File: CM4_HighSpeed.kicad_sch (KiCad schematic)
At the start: 8 parts, among them J12 THD-02-R

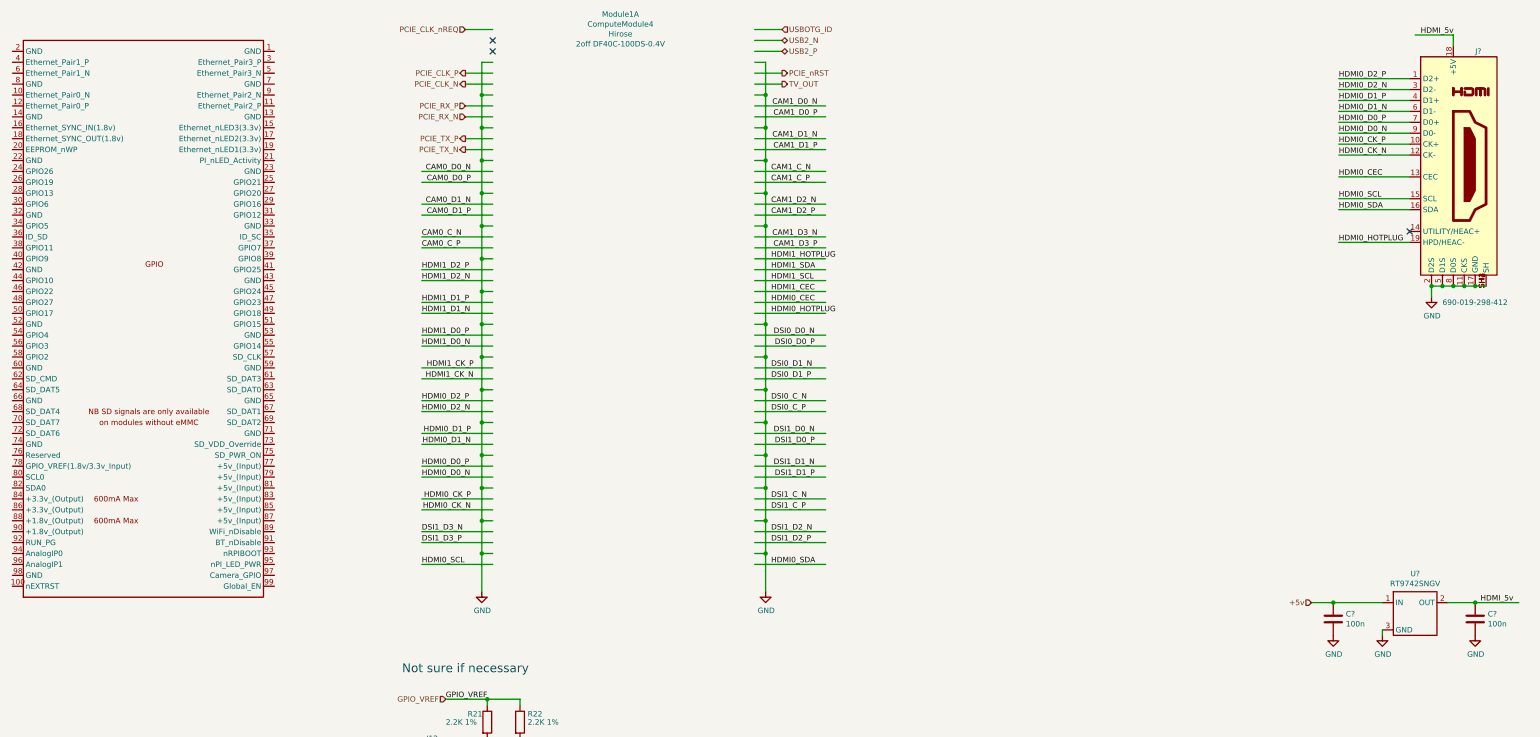
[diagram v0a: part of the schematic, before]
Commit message: Added footprints and symbols
Could not find -on SnapEDA- MCWR06X3322FTL, MCMR06X3162FTL and USB-A-S-VT.
Power load switch NCP380HSN05AAT1G only had footprint on SnapEDA, no symbol.
Need to update HMDI footprint and symbol to correct one.
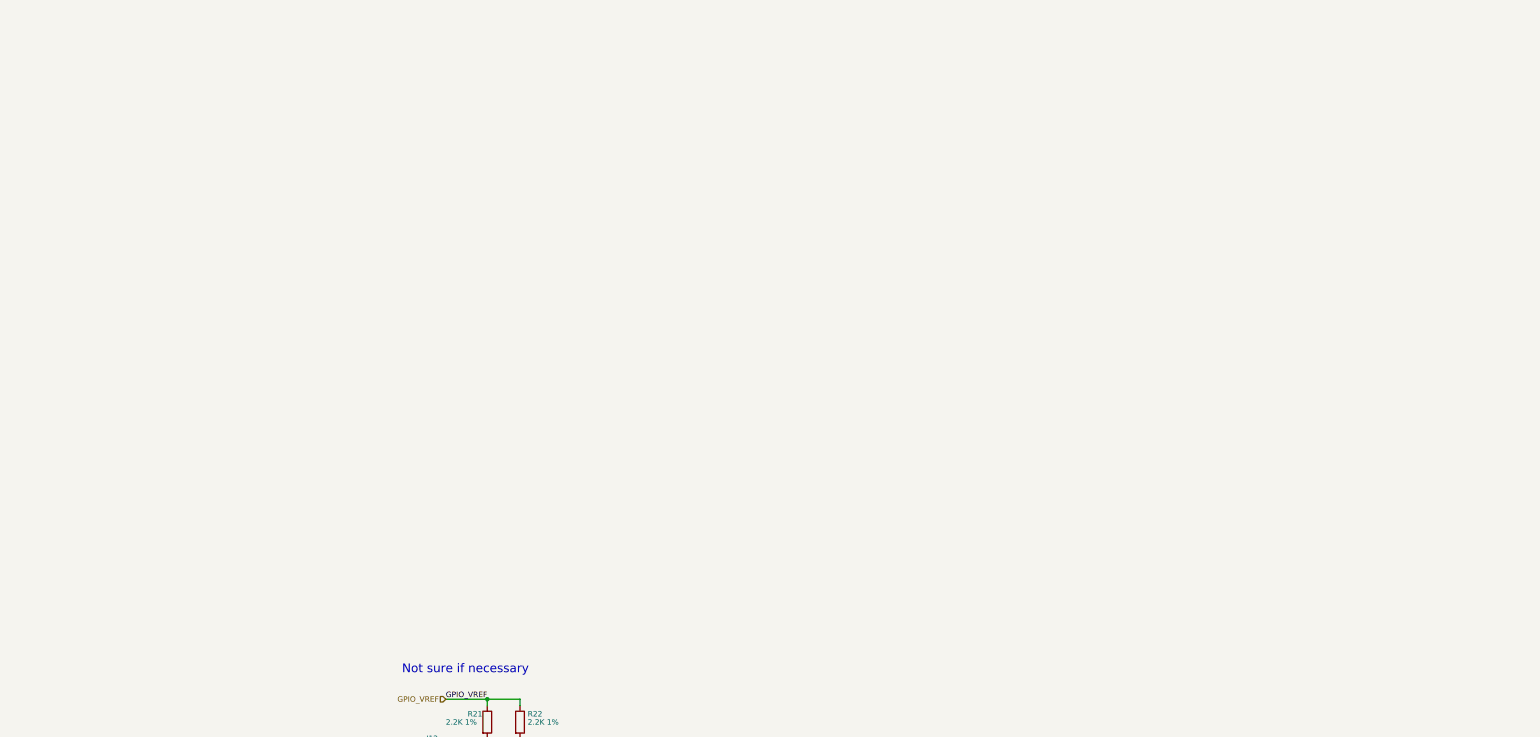
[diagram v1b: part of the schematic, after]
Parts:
- removed C? (x2): 100n, Capacitor_SMD:C_0402_1005Metric, symbol Device:C
- removed J?: 690-019-298-412, CM4IO:EDAC 690-019-298-412, symbol CM4IO:HDMI_A_1.4
- removed Module1: ComputeModule4, CM4IO:Raspberry-Pi-4-Compute-Module, symbol CM4IO:ComputeModule4-CM4
- removed U?: RT9742SNGV, Package_TO_SOT_SMD:SOT-23, symbol CM4IO:RT9742SNGV
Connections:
- no-connect marks 3 -> 0

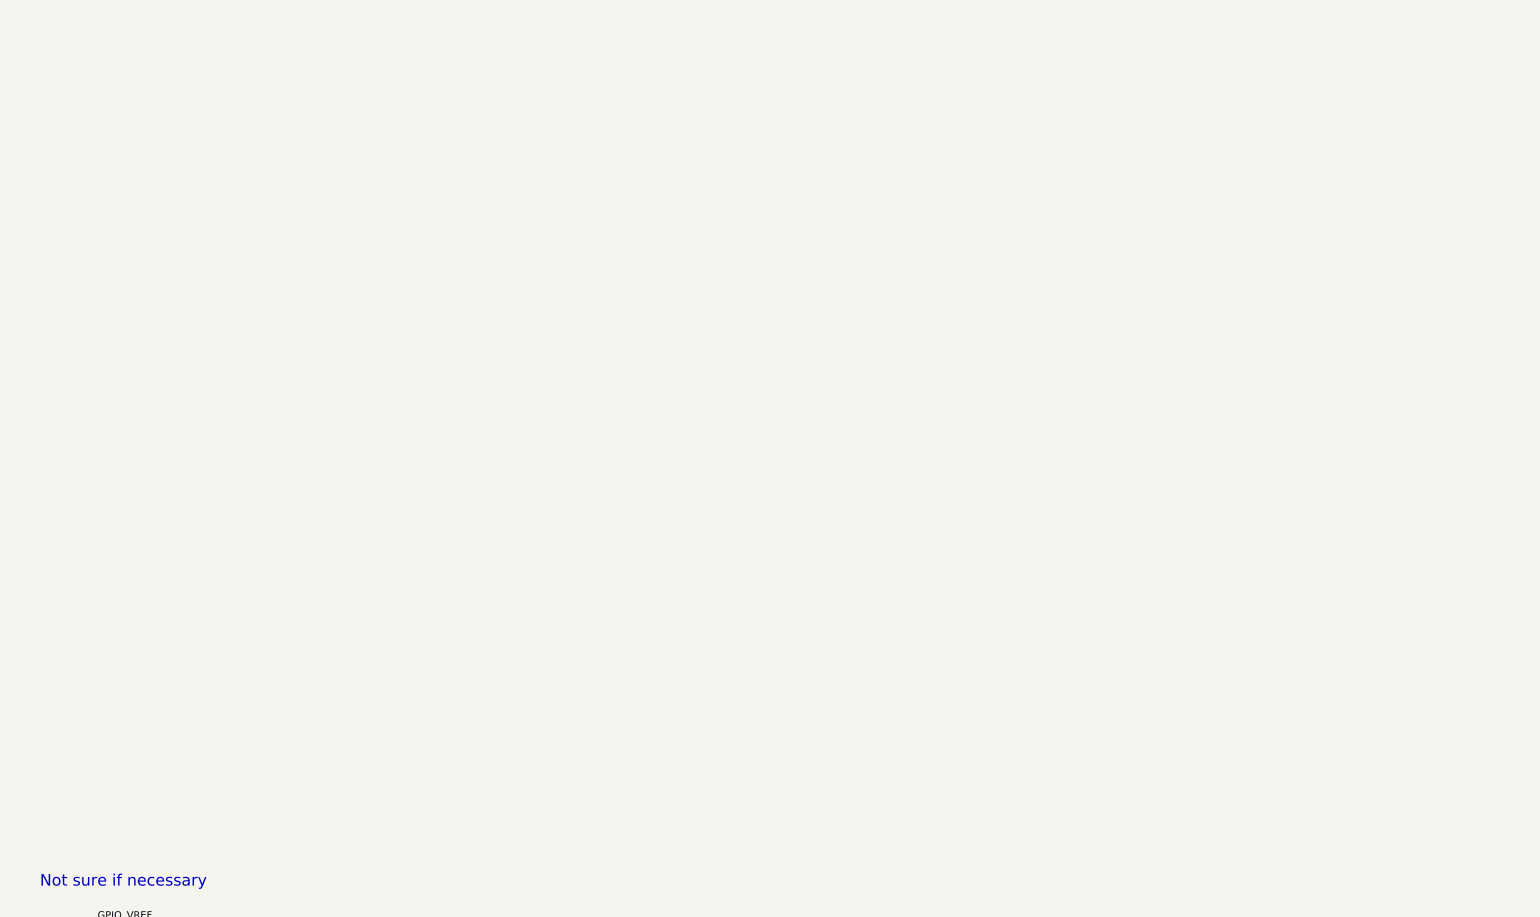
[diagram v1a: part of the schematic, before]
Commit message: Added footprints for PCIe and added busses for PCIe and Ethernet
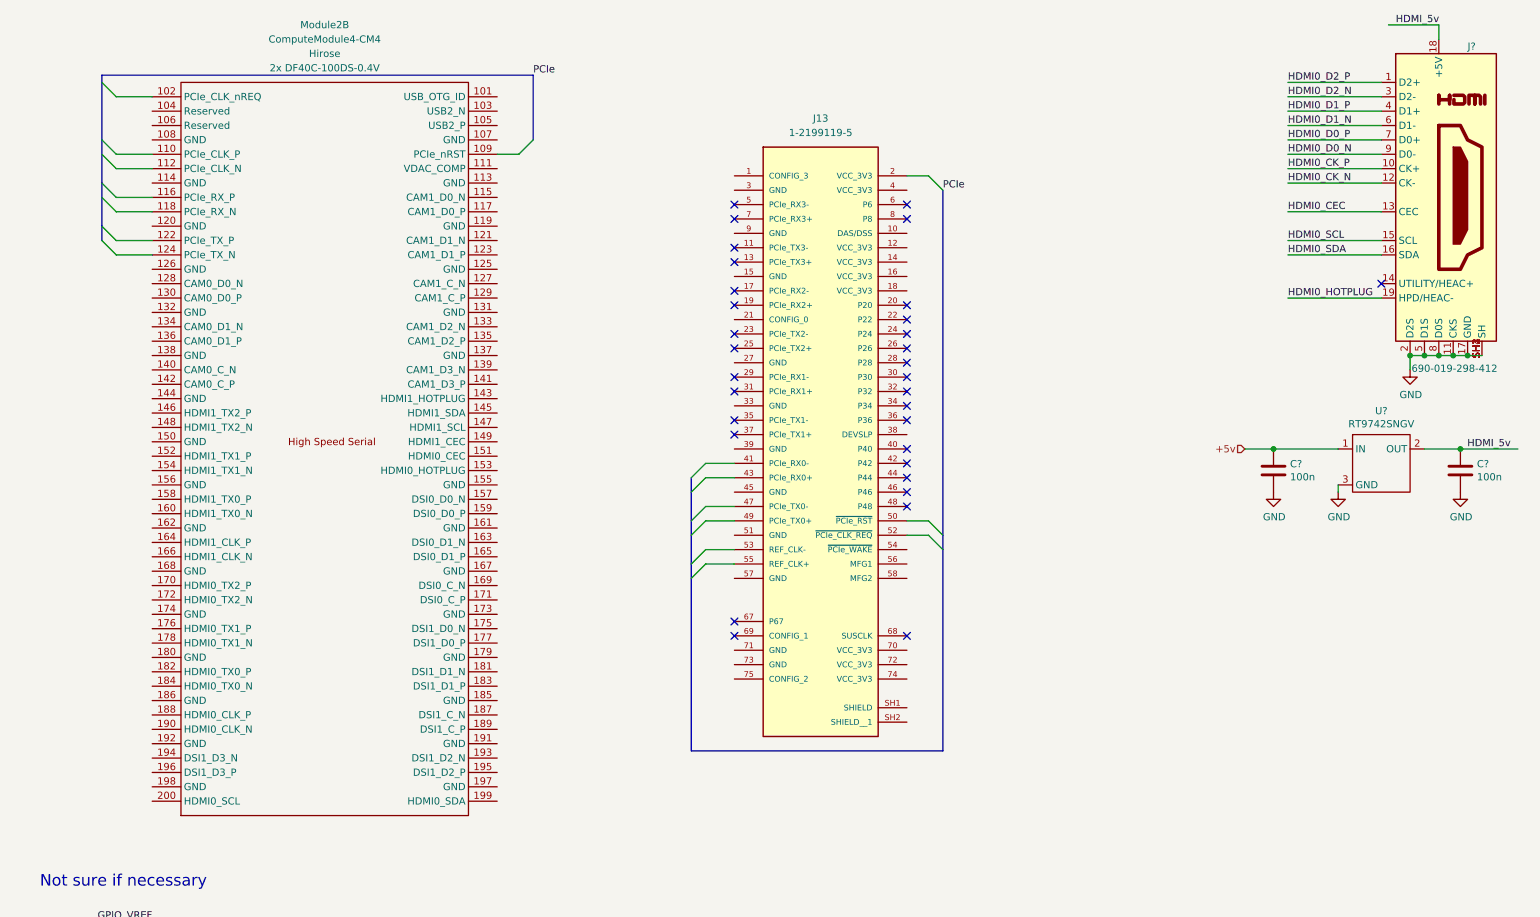
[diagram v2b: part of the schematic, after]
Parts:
- added C? (x2): 100n, Capacitor_SMD:C_0402_1005Metric, symbol Device:C
- added J13: 1-2199119-5, lib:TE_1-2199119-5, symbol 1-2199119-5_Finley:1-2199119-5
- added J?: 690-019-298-412, CM4IO:EDAC 690-019-298-412, symbol CM4IO:HDMI_A_1.4
- added Module2: ComputeModule4-CM4, CM4IO:Raspberry-Pi-4-Compute-Module, symbol CM4IO:ComputeModule4-CM4
- added U?: RT9742SNGV, Package_TO_SOT_SMD:SOT-23, symbol CM4IO:RT9742SNGV
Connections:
- new net +5v: C?.1, U?.1 (IN)
- new net GND: C?.2, C?.2, J?.11 (CKS), J?.17 (GND), J?.2 (D2S), J?.5 (D1S), J?.8 (D0S), J?.SH1 (SH), J?.SH2 (SH), J?.SH3 (SH), J?.SH4 (SH), U?.3 (GND)
- new net HDMI0_CEC: J?.13 (CEC)
- new net HDMI0_CK_N: J?.12 (CK-)
- new net HDMI0_CK_P: J?.10 (CK+)
- new net HDMI0_D0_N: J?.9 (D0-)
- new net HDMI0_D0_P: J?.7 (D0+)
- new net HDMI0_D1_N: J?.6 (D1-)
- new net HDMI0_D1_P: J?.4 (D1+)
- new net HDMI0_D2_N: J?.3 (D2-)
- new net HDMI0_D2_P: J?.1 (D2+)
- new net HDMI0_HOTPLUG: J?.19 (HPD/HEAC-)
- new net HDMI0_SCL: J?.15 (SCL)
- new net HDMI0_SDA: J?.16 (SDA)
- new net HDMI_5v: C?.1, J?.18 (+5V), U?.2 (OUT)
- no-connect marks 0 -> 32

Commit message: Cleaned up schematics and added gnds and no-connects
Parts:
- added J14: USB_A, Connector_USB:USB_A_Receptacle_XKB_U231-091N-4BLRA00-S, symbol Connector:USB_A
- added J15: USB_OTG, Connector_USB:USB_Micro-B_Amphenol_10103594-0001LF_Horizontal, symbol Connector:USB_OTG
- added J16: Conn_01x02, symbol Connector_Generic:Conn_01x02
- added J2: SS-52400-004, SS-52400-004:STEWART_SS-52400-004 (USB-C), symbol SS-52400-004:SS-52400-004
- added U11: TPD4EUSB30, Package_SON:USON-10_2.5x1.0mm_P0.5mm, symbol CM4IO:TPD4EUSB30
- J13: footprint lib:TE_1-2199119-5 -> M2Key:TE_1-2199119-5
- J5: renamed from J?; footprint CM4IO:EDAC 690-019-298-412 -> HMDI:AMPHENOL_10029449-111RLF
- Module2: footprint CM4IO:Raspberry-Pi-4-Compute-Module -> ComputeModule4:Raspberry-Pi-4-Compute-Module
- gave numbers to parts that had none: 3
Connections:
- net HDMI0_CEC is gone; now on net H9: J5.13 (CEC)
- net HDMI0_CK_N is gone; now on net H8: J5.12 (CK-)
- net HDMI0_CK_P is gone; now on net H7: J5.10 (CK+)
- net HDMI0_D0_N is gone; now on net H6: J5.9 (D0-)
- net HDMI0_D0_P is gone; now on net H5: J5.7 (D0+)
- net HDMI0_D1_N is gone; now on net H4: J5.6 (D1-)
- net HDMI0_D1_P is gone; now on net H3: J5.4 (D1+)
- net HDMI0_D2_N is gone; now on net H2: J5.3 (D2-)
- net HDMI0_D2_P is gone; now on net H1: J5.1 (D2+)
- net HDMI0_HOTPLUG is gone; now on net H12: J5.19 (HPD/HEAC-)
- net HDMI0_SCL is gone; now on net H10: J5.15 (SCL)
- net HDMI0_SDA is gone; now on net H11: J5.16 (SDA)
- net +5v: now also J14.1 (VBUS), J15.1 (VBUS)
- net GND: now also J13.1 (CONFIG_3), J13.15 (GND), J13.21 (CONFIG_0), J13.27 (GND), J13.3 (GND), J13.33 (GND), J13.39 (GND), J13.45 (GND), J13.51 (GND), J13.57 (GND), J13.71 (GND), J13.73 (GND), J13.9 (GND), J13.SH1 (SHIELD), J13.SH2 (SHIELD__1), Module2.107 (GND), Module2.108 (GND), Module2.113 (GND), Module2.114 (GND), Module2.119 (GND), Module2.120 (GND), Module2.125 (GND), Module2.126 (GND), Module2.131 (GND), Module2.132 (GND), Module2.137 (GND), Module2.138 (GND), Module2.144 (GND), Module2.150 (GND), Module2.155 (GND), Module2.156 (GND), Module2.161 (GND), Module2.162 (GND), Module2.167 (GND), Module2.168 (GND), Module2.173 (GND), Module2.174 (GND), Module2.179 (GND), Module2.180 (GND), Module2.185 (GND), Module2.186 (GND), Module2.191 (GND), Module2.192 (GND), Module2.197 (GND), Module2.198 (GND), J14.4 (GND), J14.5 (Shield), J15.5 (GND), J15.6 (Shield), J16.1 (Pin_1), U11.3 (GND), U11.8 (GND)
- net USB_OTG: now reaches Module2.101 (USB_OTG_ID)
- net USB_OTG: now also J15.4 (ID), J16.2 (Pin_2)
- net P7: now reaches Module2.102 (PCIe_CLK_nREQ)
- net P7: now also J13.12 (VCC_3V3), J13.14 (VCC_3V3), J13.16 (VCC_3V3), J13.18 (VCC_3V3), J13.2 (VCC_3V3), J13.4 (VCC_3V3), J13.50 (~{PCIe_RST}), J13.52 (~{PCIe_CLK_REQ}), J13.70 (VCC_3V3), J13.72 (VCC_3V3), J13.74 (VCC_3V3), Module2.109 (PCIe_nRST)
- net USBD-: now reaches Module2.103 (USB2_N)
- net USBD-: now also U11.2 (D1-), U11.9
- net USBD+: now reaches Module2.105 (USB2_P)
- net USBD+: now also U11.1 (D1+), U11.10
- net P6: now reaches Module2.110 (PCIe_CLK_P)
- net P6: now also J13.55 (REF_CLK+)
- net P5: now reaches Module2.112 (PCIe_CLK_N)
- net P5: now also J13.53 (REF_CLK-)
- net P2: now reaches Module2.116 (PCIe_RX_P)
- net P2: now also J13.43 (PCIe_RX0+)
- net P1: now reaches Module2.118 (PCIe_RX_N)
- net P1: now also J13.41 (PCIe_RX0-)
- net P4: now reaches Module2.122 (PCIe_TX_P)
- net P4: now also J13.49 (PCIe_TX0+)
- net P3: now reaches Module2.124 (PCIe_TX_N)
- net P3: now also J13.47 (PCIe_TX0-)
- net H9: now reaches Module2.151 (HDMI0_CEC)
- net H12: now reaches Module2.153 (HDMI0_HOTPLUG)
- net H1: now reaches Module2.170 (HDMI0_TX2_P)
- net H2: now reaches Module2.172 (HDMI0_TX2_N)
- net H3: now reaches Module2.176 (HDMI0_TX1_P)
- net H4: now reaches Module2.178 (HDMI0_TX1_N)
- net H5: now reaches Module2.182 (HDMI0_TX0_P)
- net H6: now reaches Module2.184 (HDMI0_TX0_N)
- net H7: now reaches Module2.188 (HDMI0_CLK_P)
- net H8: now reaches Module2.190 (HDMI0_CLK_N)
- net H11: now reaches Module2.199 (HDMI0_SDA)
- net H10: now reaches Module2.200 (HDMI0_SCL)
- new net: J2.SH1 (SHIELD), J2.SH2 (SHIELD), J2.SH3 (SHIELD), J2.SH4 (SHIELD)
- new net GND_A: J2.A1 (GND_A), J2.A12 (GND_A)
- new net GND_B: J2.B1 (GND_B), J2.B12 (GND_B)
- new net VBUS_A: J2.A4 (VBUS_A), J2.A9 (VBUS_A)
- new net VBUS_B: J2.B4 (VBUS_B), J2.B9 (VBUS_B)
- new net pUSBD+: J14.3 (D+), J15.3 (D+), U11.4 (D2+), U11.7
- new net pUSBD-: J14.2 (D-), J15.2 (D-), U11.5 (D2-), U11.6
- no-connect marks 32 -> 85
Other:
- note added: "Eventueel extra pull_up (word al intern gedaan)"
- note added: "Niet zeker of Shield naar GND moet."
- note added: "USB ESD protection"
- note added: "USB-c connector"
- moved on the sheet: J13
